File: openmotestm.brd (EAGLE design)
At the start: 24.4 x 34 mm, 49 parts

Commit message: right position in brd.
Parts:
- moved C3 147.6 mm to (56.1, 187.3), flipped to the bottom
- moved U$5 146.6 mm to (54.7, 184.9), flipped to the bottom
- moved C12 145.9 mm to (53.7, 193.0), flipped to the bottom
- moved C13 145.9 mm to (53.7, 191.1), flipped to the bottom
- moved C10 145.4 mm to (53.1, 197.0), flipped to the top
- moved C4 145.4 mm to (53.1, 207.1), flipped to the top
- moved C5 145.4 mm to (53.1, 204.6), flipped to the top
- moved C7 145.4 mm to (53.1, 199.5), flipped to the top
- moved C9 145.4 mm to (53.1, 194.4), flipped to the top
- moved C6 145.4 mm to (53.1, 202.1), flipped to the top
- moved C8 145.4 mm to (53.1, 191.9), flipped to the top
- moved C19 143.8 mm to (50.5, 197.0), flipped to the bottom
- moved C21 143.5 mm to (49.9, 205.2), flipped to the bottom
- moved C23 143.5 mm to (49.9, 210.3), flipped to the bottom
- moved C20 143.1 mm to (49.3, 202.7), flipped to the bottom
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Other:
- outline, holes or cut-outs redrawn

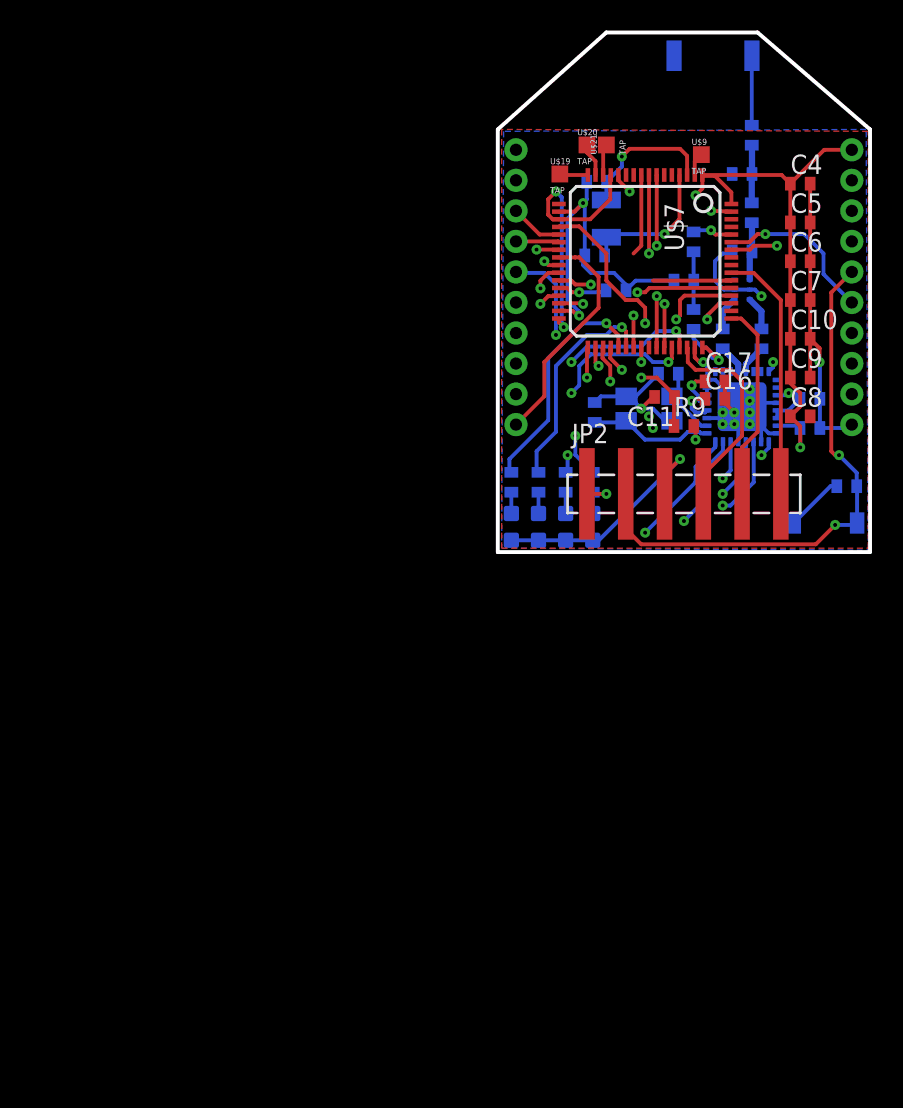
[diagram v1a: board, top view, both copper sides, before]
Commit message: change the footprint of capacity larger than 1uF to 0603 footprint. Update 3D sketchUp model
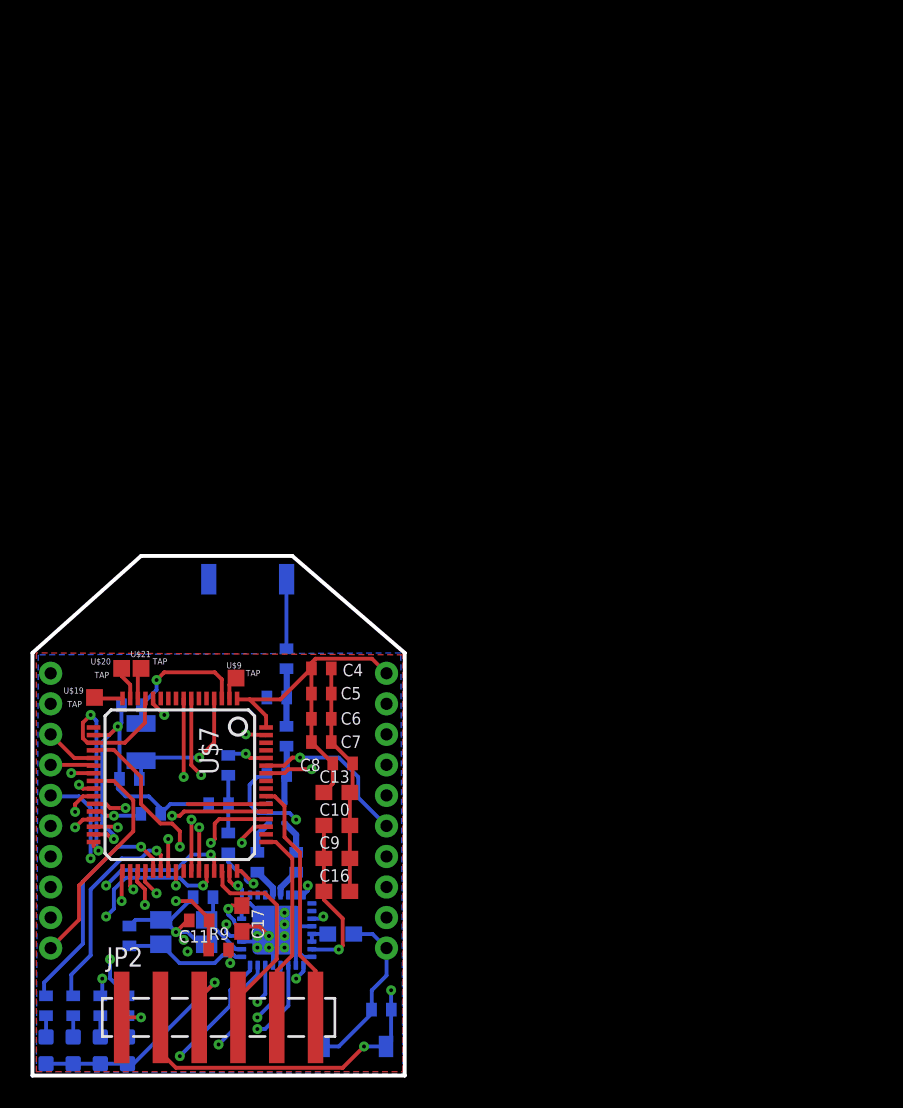
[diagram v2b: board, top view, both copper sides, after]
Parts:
- C10, C12, C13, C16, C17, C9: device rcl:C0402 -> rcl:C0603
- moved C17 46.9 mm to (16.5, 159.0), turned to 270 degrees
- moved C12 46.6 mm to (23.0, 158.0)
- moved U$5 46.1 mm to (23.9, 150.6)
- moved C1 45.9 mm to (9.27, 173.0)
- moved C14 45.9 mm to (9.14, 157.9)
- moved C20 45.9 mm to (18.8, 168.4)
- moved C23 45.9 mm to (19.4, 176.0)
- moved JP2 45.9 mm to (8.64, 152.5)
- moved R3 45.9 mm to (15.6, 164.0)
- moved R5 45.9 mm to (9.02, 153.3)
- moved R6 45.9 mm to (7.24, 153.3)
- moved R7 45.9 mm to (5.46, 153.3)
- moved R8 45.9 mm to (3.68, 153.3)
- moved U$3 45.9 mm to (18.8, 158.2)
- moved C15 45.9 mm to (14.0, 160.4)
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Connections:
- removed net PC1: U$7.9
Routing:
- net PC1: track 5.35 -> 0.00 mm
- net VCC: track 66.1 -> 62.1 mm, vias 7 -> 6
- net GND: track 108.2 -> 109.8 mm, vias 10 -> 9
- net N$15: track 2.31 -> 1.54 mm
- net JTDO/SWO: track 16.7 -> 16.2 mm

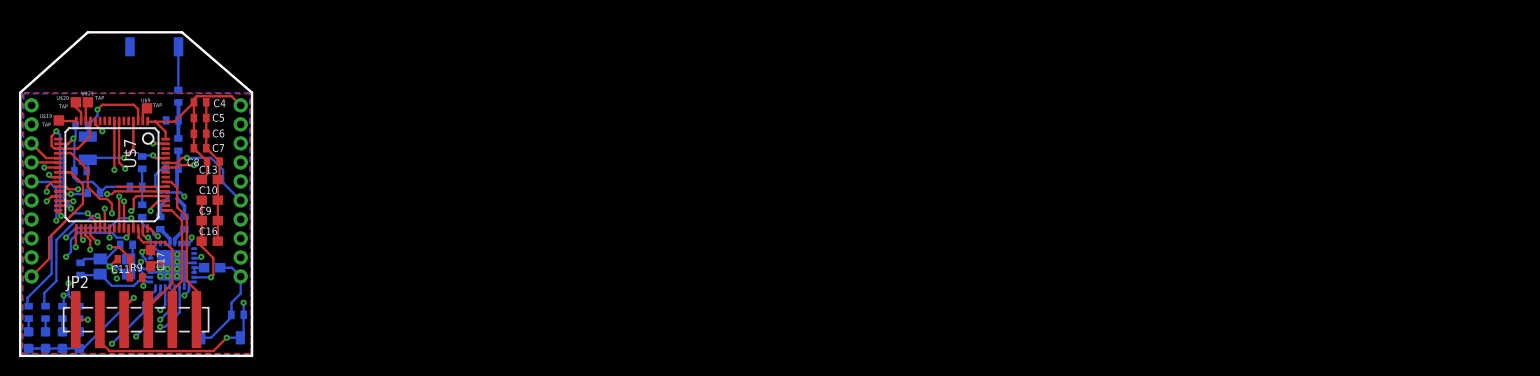
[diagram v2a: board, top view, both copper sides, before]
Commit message: change the pcb to satisfy minimum clearance of 5 mil
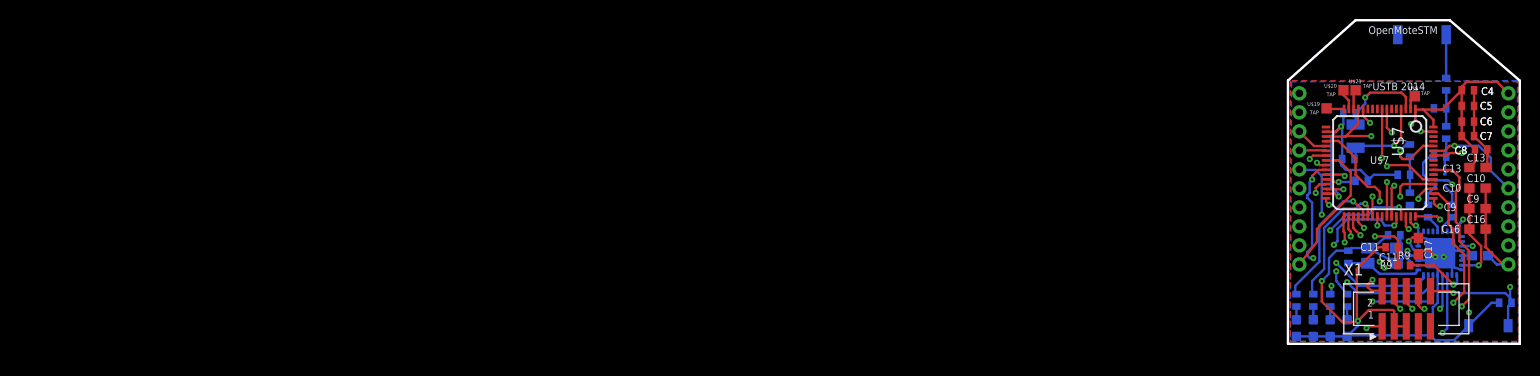
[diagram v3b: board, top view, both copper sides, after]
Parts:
- removed JP2: JTAG-CONNECTER, SparkFun-Connectors:1X06_SMD_MALE
- added X1: PHB_1MM27_2X05_SNS, _hhn_con_pinhead_box_1mm27:PHB_1MM27_2X05_SNS
- moved C1 133.4 mm to (142.6, 174.2)
- moved C17 133.4 mm to (149.9, 160.3)
- moved C4 133.4 mm to (155.1, 176.7)
- moved C5 133.4 mm to (155.1, 175.0)
- moved C6 133.4 mm to (155.1, 173.4)
- moved C7 133.4 mm to (155.1, 171.8)
- moved R2 133.4 mm to (148.3, 167.8)
- moved R9 133.4 mm to (148.3, 158.2)
- moved U$2 133.4 mm to (150.2, 182.5)
- moved U$8 133.4 mm to (148.3, 156.3)
- moved U$9 133.4 mm to (149.5, 176.0)
- moved C10 133.4 mm to (156.1, 166.4)
- moved C11 133.4 mm to (147.1, 160.1)
- moved C12 133.4 mm to (156.3, 159.3)
- moved C13 133.4 mm to (156.1, 168.5)
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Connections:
- new net N$32: X1.7
- new net NC: X1.9
- net GND: now also X1.3, X1.5; no longer JP2.3
- net JTCK-SWCLK: now also X1.4; no longer JP2.5
- net JTDI: now also X1.8
- net JTDO/SWO: now also X1.6; no longer JP2.6
- net JTMS-SWDIO: now also X1.2; no longer JP2.4
- net RESET: now also X1.10; no longer JP2.2
- net VCC: now also X1.1; no longer JP2.1, R3.1
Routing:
- net GND: track 109.8 -> 156.9 mm, vias 9 -> 10
- net JTDI: track 0.00 -> 19.2 mm, vias 0 -> 2
- net JTCK-SWCLK: track 13.0 -> 24.5 mm, vias 0 -> 3
- net RESET: track 54.8 -> 43.5 mm
- net JTDO/SWO: track 16.2 -> 26.1 mm, vias 0 -> 2
- net RF_IRQ: track 29.4 -> 20.8 mm
- net RF_CLKM: track 15.6 -> 24.2 mm, vias 2 -> 3
- net VCC: track 62.1 -> 70.1 mm, vias 6 -> 7
- net PA7: track 6.56 -> 12.1 mm
- net PD2: track 5.15 -> 0.00 mm
- net RF_SCLK: track 21.8 -> 26.4 mm
- net RF_MISO: track 19.4 -> 23.5 mm
- net RF_/SEL: track 21.5 -> 17.7 mm
- net N$3: track 2.64 -> 6.11 mm
- net RF_MOSI: track 16.5 -> 18.5 mm
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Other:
- board text added: "AN2051"
- board text added: "C1"
- board text added: "C10"
- board text added: "C11"
- board text added: "C12"
- board text added: "C13"
- board text added: "C14"
- board text added: "C15"
- board text added: "C16"
- board text added: "C18"
- board text added: "C19"
- board text added: "C2"
- board text added: "C20"
- board text added: "C21"
- board text added: "C22"
- board text added: "C23"
- board text added: "C3"
- board text added: "C4"
- board text added: "C5"
- board text added: "C6"
- board text added: "C7"
- board text added: "C8"
- board text added: "C9"
- board text added: "D1"
- board text added: "D2"
- board text added: "D3"
- board text added: "D4"
- board text added: "OpenMoteSTM"
- board text added: "R1"
- board text added: "R2"
- board text added: "R3"
- board text added: "R4"
- board text added: "R5"
- board text added: "R6"
- board text added: "R7"
- board text added: "R8"
- board text added: "R9"
- board text added: "U$1"
- board text added: "U$2"
- board text added: "U$3"
- board text added: "U$4"
- board text added: "U$5"
- board text added: "U$6"
- board text added: "U$7"
- board text added: "USTB 2014"

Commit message: update openmotestm
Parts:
- moved U$6 215.6 mm to (-1.27, 1.78)
- moved C1 215.6 mm to (-4.70, 16.8)
- moved C10 215.6 mm to (8.76, 8.89)
- moved C11 215.6 mm to (-0.25, 2.67)
- moved C12 215.6 mm to (9.02, 1.78)
- moved C13 215.6 mm to (8.76, 11.0)
- moved C14 215.6 mm to (-4.83, 1.65)
- moved C15 215.6 mm to (0.00, 3.94)
- moved C16 215.6 mm to (8.76, 4.57)
- moved C17 215.6 mm to (2.54, 2.79)
- moved C18 215.6 mm to (3.56, 6.48)
- moved C19 215.6 mm to (6.10, 6.48)
- moved C2 215.6 mm to (-4.83, 11.9)
- moved C20 215.6 mm to (4.83, 12.2)
- moved C21 215.6 mm to (5.46, 14.7)
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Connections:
- net VCC: now also R3.1
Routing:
- net VCC: track 70.1 -> 73.3 mm, vias 7 -> 8
- net N$4: track 3.79 -> 6.42 mm
- net N$3: track 6.11 -> 7.44 mm
- net GND: track 156.9 -> 157.8 mm

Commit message: drawing quadcopter
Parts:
- moved C23 7.76 mm to (4.95, 12.1)
- moved U$9 7.76 mm to (1.65, 10.8)
- moved C10 7.76 mm to (8.26, 1.14)
- moved C2 7.76 mm to (-5.33, 4.19)
- moved C3 7.76 mm to (11.2, -10.9)
- moved C7 7.76 mm to (7.24, 6.60)
- moved C8 7.76 mm to (8.64, 5.21)
- moved D1 7.76 mm to (-5.46, -13.6)
- moved D2 7.76 mm to (-7.24, -13.6)
- moved D3 7.76 mm to (-9.02, -13.6)
- moved D4 7.76 mm to (-10.8, -13.6)
- moved R1 7.76 mm to (1.14, 6.22)
- moved R3 7.76 mm to (1.14, 1.52)
- moved U$1 7.76 mm to (-4.57, 6.60)
- moved U$5 7.76 mm to (9.40, -13.3)
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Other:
- outline, holes or cut-outs redrawn

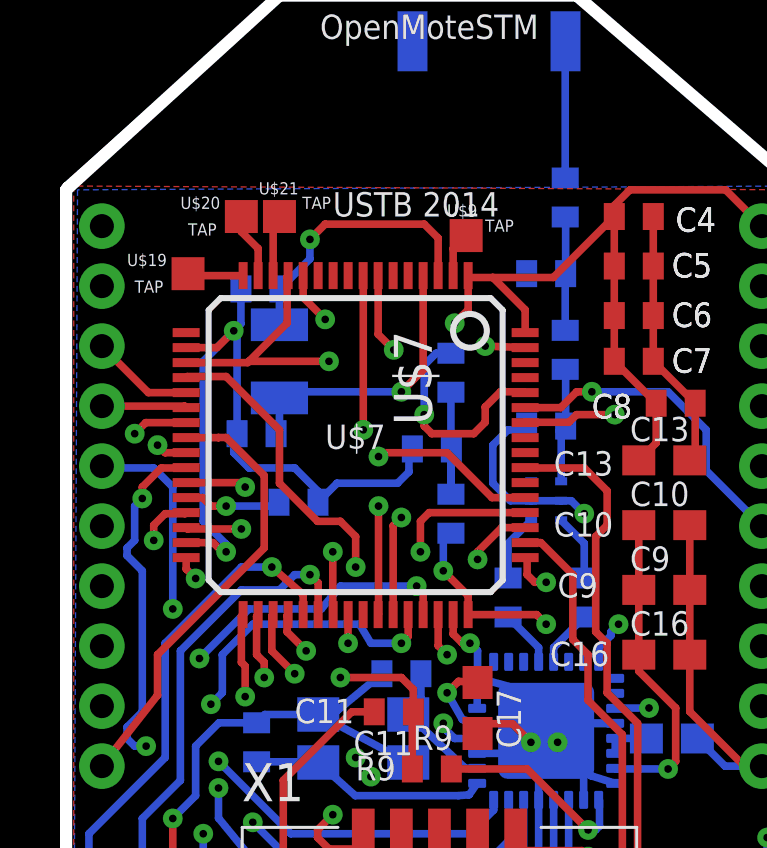
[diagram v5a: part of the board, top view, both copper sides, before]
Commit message: Add XBee-Explorer-Dongle-Sparkfun. Update openmotestm. arrange the layout of openquadcopter board.
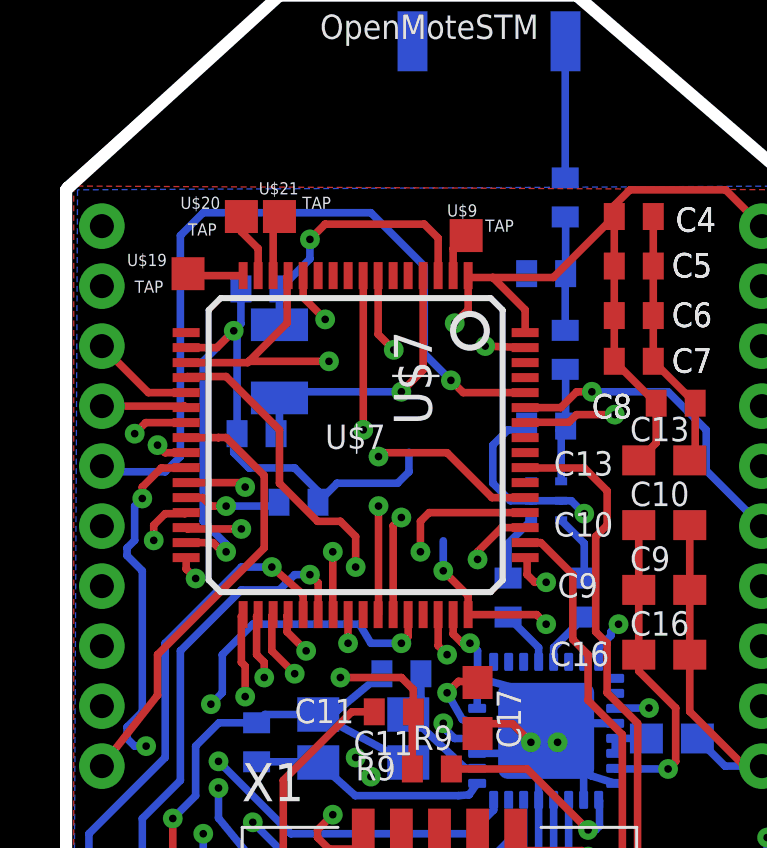
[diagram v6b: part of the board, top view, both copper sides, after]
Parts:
- removed R1, R2, R3: 5K, rcl:R0402
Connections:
- removed net N$3: R1.1, U$7.60
- removed net N$4: R1.2, R2.1, R3.2
- new net BOOT0: U$7.60, U$8.16
- net GND: no longer R2.2
- net PA12: no longer U$8.16
- net PC9: no longer U$8.9
- net RESET: now also U$8.9
- net VCC: no longer R3.1
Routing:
- net BOOT0: track 0.00 -> 26.3 mm, vias 0 -> 1
- net PA12: track 18.4 -> 0.00 mm, vias 3 -> 0
- net N$3: track 7.44 -> 0.00 mm, vias 1 -> 0
- net N$4: track 6.42 -> 0.00 mm
- net RESET: track 43.5 -> 46.0 mm
- net PC9: track 15.6 -> 14.6 mm
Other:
- board text removed: "USTB 2014"

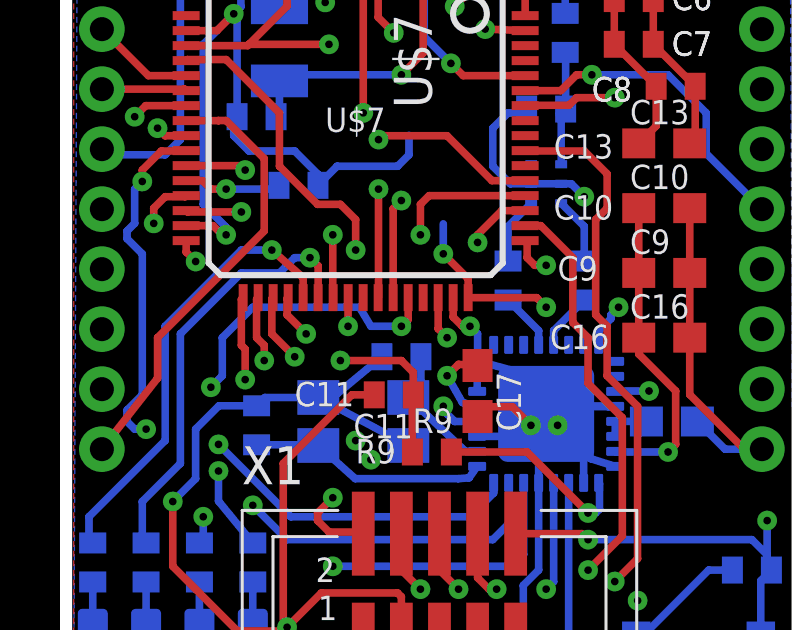
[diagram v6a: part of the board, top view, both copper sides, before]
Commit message: remove unused route
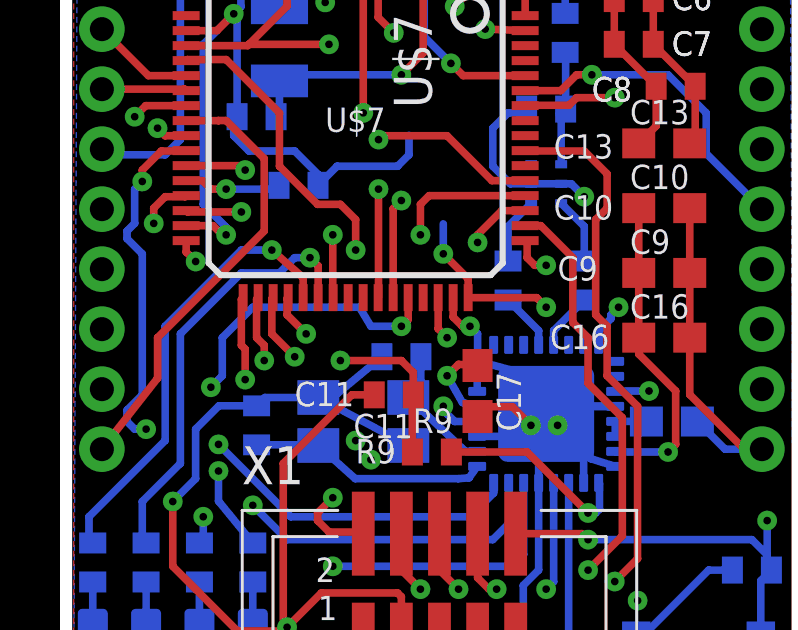
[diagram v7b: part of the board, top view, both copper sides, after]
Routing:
- net PC9: track 14.6 -> 0.00 mm, vias 1 -> 0
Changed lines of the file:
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@@
 <grid distance="0.05" unitdist="inch" unit="mm" style="lines" multiple="1" display="no" altdistance="0.005" altunitdist="inch" altunit="inch"/>
 <layers>
-<layer number="1" name="Top" color="4" fill="1" visible="no" active="yes"/>
-<layer number="2" name="Route2" color="1" fill="3" visible="no" active="yes"/>
+<layer number="1" name="Top" color="4" fill="1" visible="yes" active="yes"/>
+<layer number="2" name="Route2" color="1" fill="3" visible="yes" active="yes"/>
 <layer number="3" name="Route3" color="4" fill="3" visible="no" active="no"/>
 <layer number="4" name="Route4" color="1" fill="4" visible="no" active="no"/>
@@
 <layer number="13" name="Route13" color="4" fill="5" visible="no" active="no"/>
 <layer number="14" name="Route14" color="1" fill="6" visible="no" active="no"/>
-<layer number="15" name="Route15" color="4" fill="6" visible="no" active="yes"/>
+<layer number="15" name="Route15" color="4" fill="6" visible="yes" active="yes"/>
 <layer number="16" name="Bottom" color="1" fill="1" visible="yes" active="yes"/>
 <layer number="17" name="Pads" color="2" fill="1" visible="yes" active="yes"/>
@@
 <signal name="PC9">
 <contactref element="U$7" pad="40"/>
-<wire x1="10.478" y1="-4.89" x2="9.398" y2="-3.81" width="0.254" layer="15"/>
-<wire x1="9.398" y1="-3.81" x2="-1.27" y2="-3.81" width="0.254" layer="15"/>
-<wire x1="-1.27" y1="-3.81" x2="-2.286" y2="-2.794" width="0.254" layer="15"/>
-<via x="-2.286" y="-2.794" extent="1-16" drill="0.254" diameter="0.127"/>
-<wire x1="-2.286" y1="-2.794" x2="-2.286" y2="-1.844" width="0.254" layer="1"/>
-<wire x1="-2.286" y1="-1.844" x2="-2.282" y2="-1.84" width="0.254" layer="1"/>
 </signal>
 <signal name="PC4">
